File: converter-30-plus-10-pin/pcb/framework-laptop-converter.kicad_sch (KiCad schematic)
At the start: 6 parts, among them J1 20455-040E-76, J2 FFC2B28-40-G

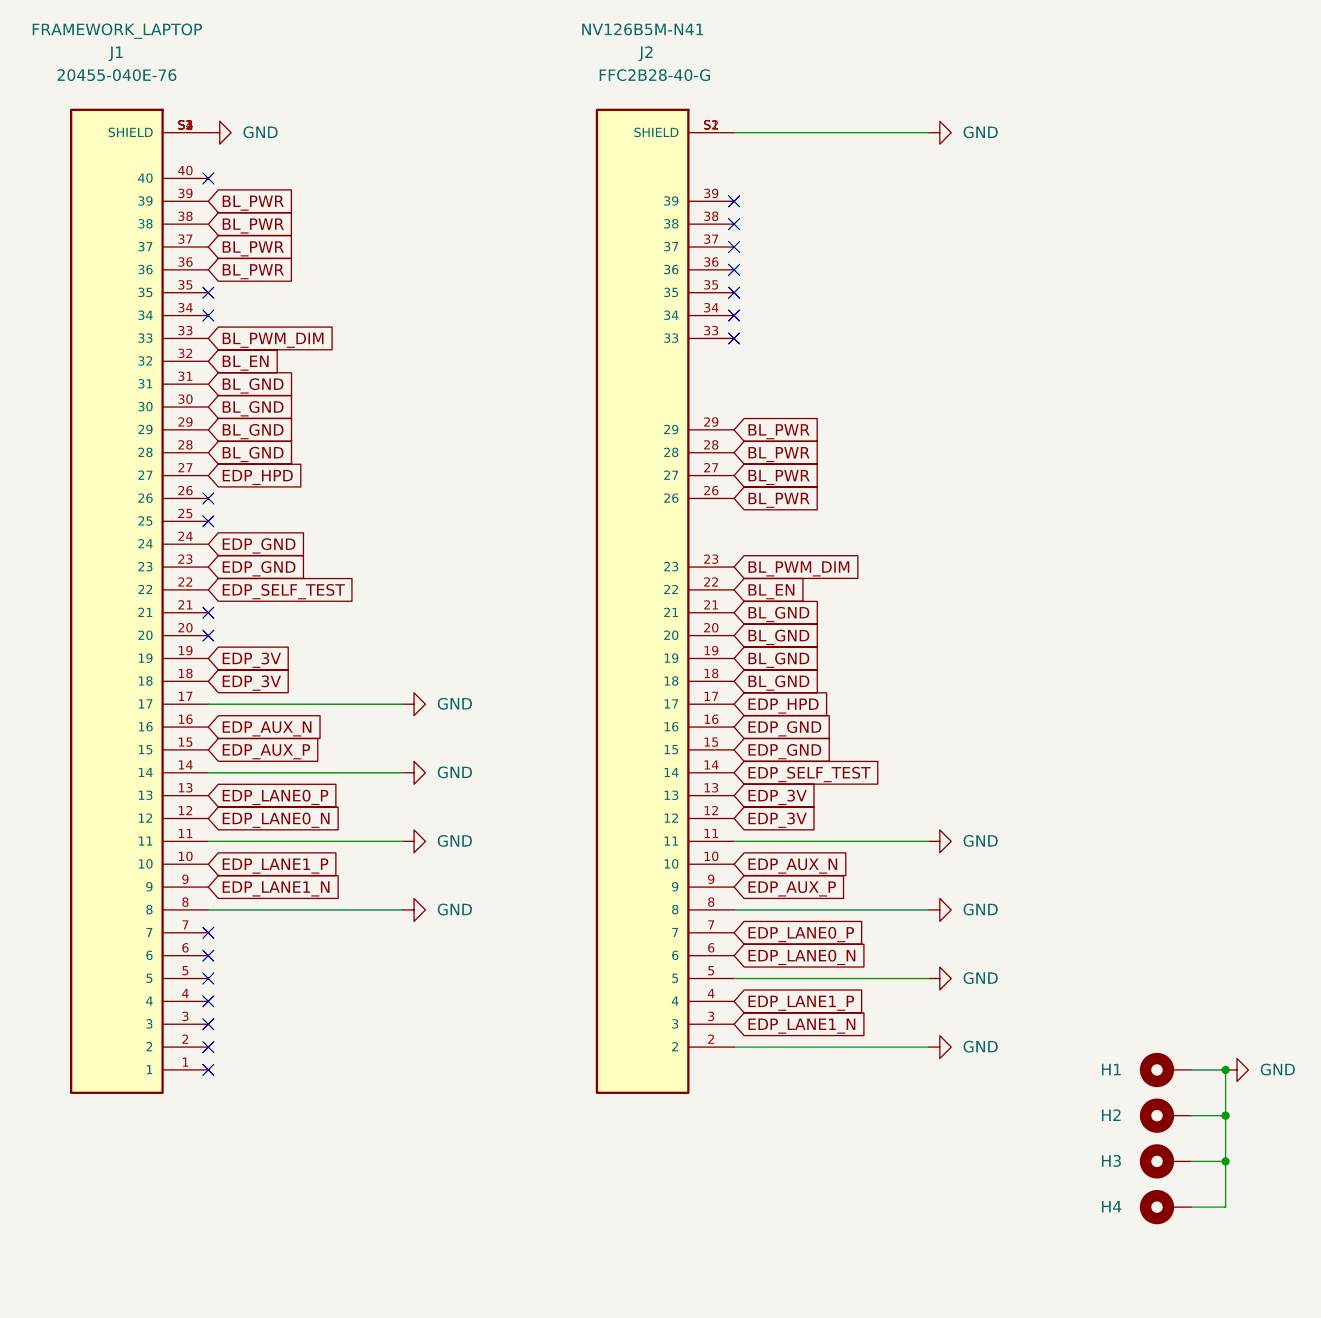
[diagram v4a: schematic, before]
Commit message: clean up converter to 2 layers & attach the BL_EN
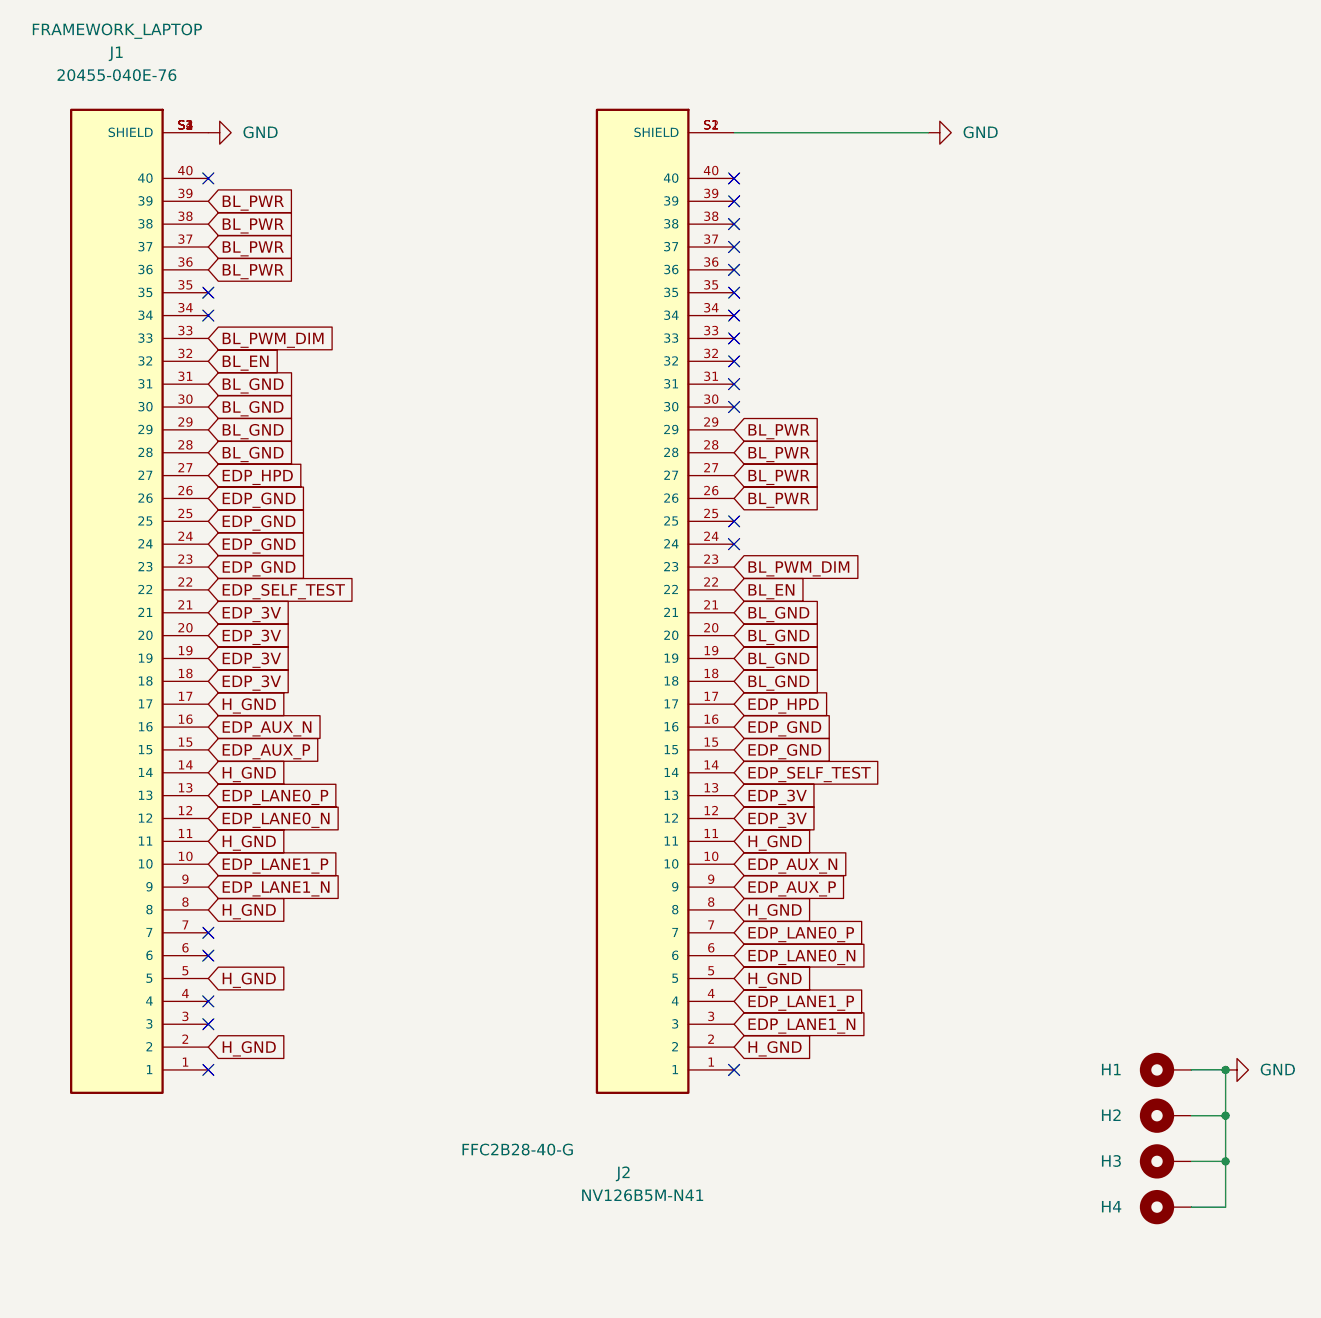
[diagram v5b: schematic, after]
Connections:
- net EDP_3V: now also J1.20, J1.21
- net EDP_GND: now also J1.25, J1.26
- net GND: no longer J1.11, J1.14, J1.17, J1.8, J2.11, J2.2, J2.5, J2.8
- net H_GND: now reaches J1.2
- net H_GND: now also J1.11, J1.14, J1.17, J1.5, J1.8, J2.11, J2.2, J2.5, J2.8
- no-connect marks 21 -> 22
